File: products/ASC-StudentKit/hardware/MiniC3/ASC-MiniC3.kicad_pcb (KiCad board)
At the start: 2 copper layers, 48 x 44 mm, 36 parts, among them J1 PUMP, J3 AUX, J4 FLOW, J5 I2C, J6 RELAY 230V, K1 HF46F/005-HS1, Q1 AO3400A, Q2 AO3400A, U1 ESP32-C3 Super Mini, U2 DS1307Z+, Y1 32.768k 12.5pF

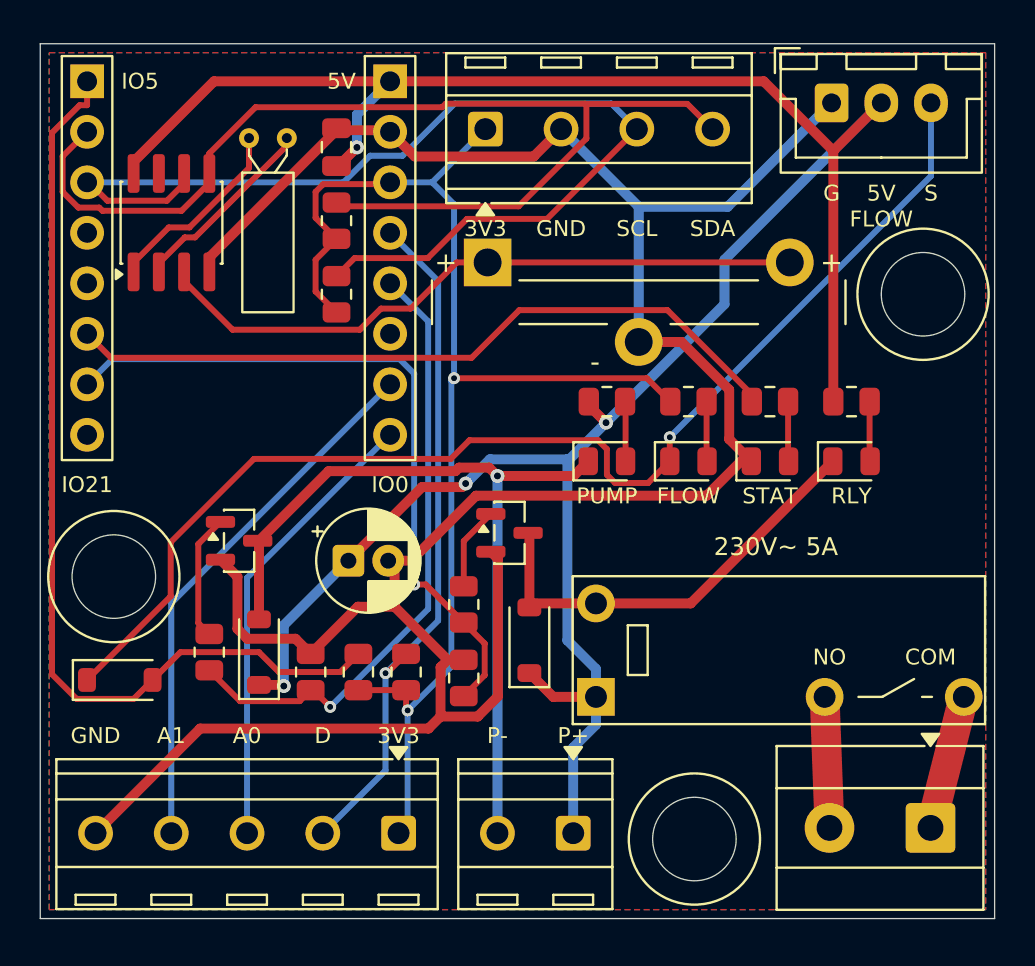
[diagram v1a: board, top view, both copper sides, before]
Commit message: ASC Mini-C3: ULN2003A driver, combo flow connector, assembly markings
- ULN2003A (LCSC C7512) drives the pump (ch 1+2) and the relay (ch 3);
  replaces 2 x AO3400A, 3 x B5819W and 4 resistors, as on FG1
- Flow input: one footprint takes a JST-XH (bench) or a 3.5 mm 3-pole
  screw terminal (FG1 field cable)
- Screw terminals now Phoenix PT-1,5 3.5 mm (KF350 type, library 3D);
  relay output is a pluggable MSTBVA 5.08 header like FG1's
- 1206 LEDs for hand soldering; ref + value labels on every part
  (R3 1K, U3 ULN2003 ...), "1" at IC pin 1, "+" at LED/diode anodes;
  back reads "Agri Sensors and Controls  Oct 2026"
- Re-routed, DRC clean (mains 5 mm), panel and fab regenerated
- Sourcing BOM: 1206 LED and ULN2003A LCSC numbers, CR2032 holder as an
  alternative to the tabbed cell; kit about Rs 967

Co-Authored-By: Claude Opus 5.5 <noreply@anthropic.com>
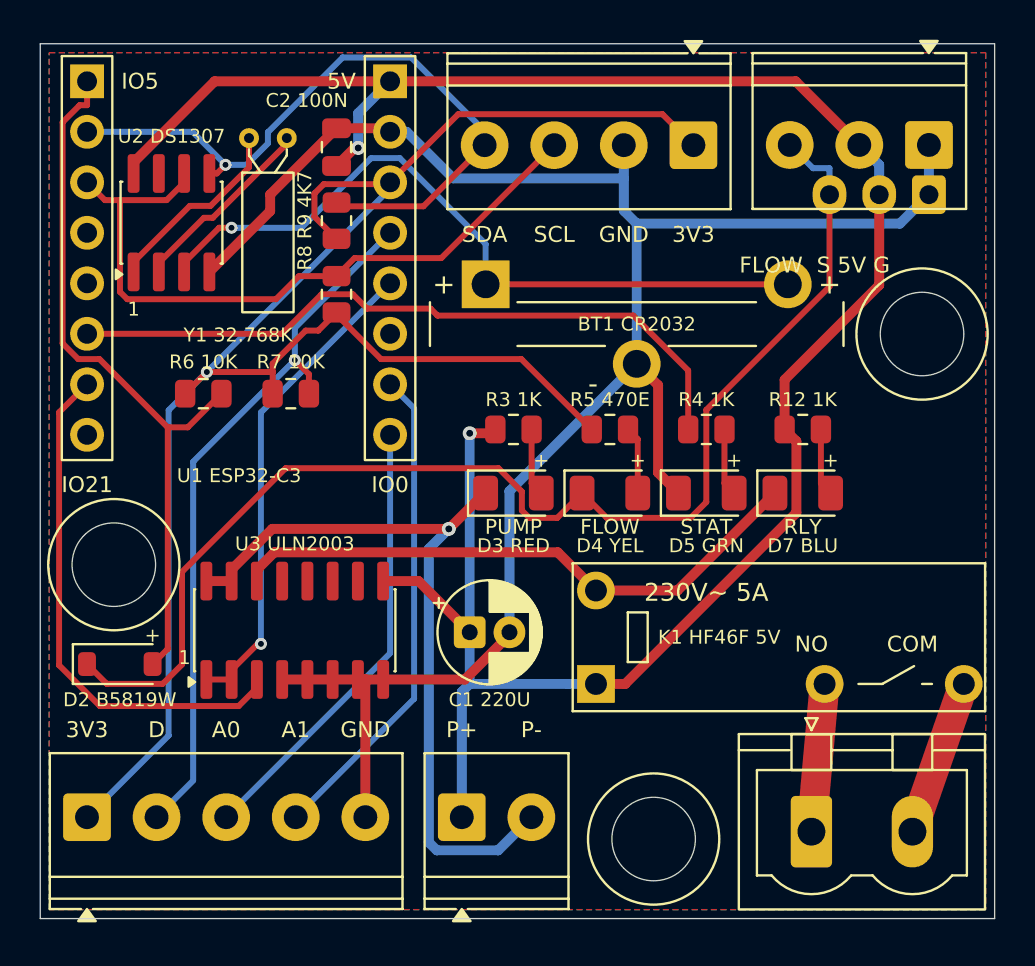
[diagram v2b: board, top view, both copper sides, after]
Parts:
- removed D1, D6: B5819W, Diode_SMD:D_SOD-123
- removed Q1, Q2: AO3400A, Package_TO_SOT_SMD:SOT-23
- removed R1, R10: 100, Resistor_SMD:R_0805_2012Metric
- removed R11, R2: 100k, Resistor_SMD:R_0805_2012Metric
- added U3: ULN2003A, Package_SO:SOIC-16_3.9x9.9mm_P1.27mm, F.Cu at (112.8, 89.5)
- D3, D4, D5, D7: footprint LED_SMD:LED_0805_2012Metric -> LED_SMD:LED_1206_3216Metric
- J1: footprint TerminalBlock_MetzConnect:TerminalBlock_MetzConnect_Type086_RT03402HBLC_1x02_P3.81mm_Horizontal -> TerminalBlock_Phoenix:TerminalBlock_Phoenix_PT-1,5-2-3.5-H_1x02_P3.50mm_Horizontal
- J3: footprint TerminalBlock_MetzConnect:TerminalBlock_MetzConnect_Type086_RT03405HBLC_1x05_P3.81mm_Horizontal -> TerminalBlock_Phoenix:TerminalBlock_Phoenix_PT-1,5-5-3.5-H_1x05_P3.50mm_Horizontal
- J4: value FLOW -> FLOW (XH or 3.5 mm); footprint Connector_JST:JST_XH_B3B-XH-A_1x03_P2.50mm_Vertical -> ASC:Flow_XH3_or_PT-1,5-3-3.5mm
- J5: footprint TerminalBlock_MetzConnect:TerminalBlock_MetzConnect_Type086_RT03404HBLC_1x04_P3.81mm_Horizontal -> TerminalBlock_Phoenix:TerminalBlock_Phoenix_PT-1,5-4-3.5-H_1x04_P3.50mm_Horizontal
- J6: value RELAY 230V -> RELAY 230V (MSTBVA); footprint TerminalBlock_MetzConnect:TerminalBlock_MetzConnect_Type101_RT01602HBWC_1x02_P5.08mm_Horizontal -> Connector_Phoenix_MSTB:PhoenixContact_MSTBVA_2,5_2-G-5,08_1x02_P5.08mm_Vertical
- moved R6 16.0 mm to (108.2, 77.6), turned to 0 degrees
- moved J3 15.7 mm to (102.3, 98.9), turned to 0 degrees
- moved R7 15.2 mm to (112.6, 77.6), turned to 0 degrees
- moved J5 10.5 mm to (132.8, 65.1), turned to 180 degrees
- moved C1 7.08 mm to (121.6, 89.6)
- moved J6 5.99 mm to (138.8, 99.6), turned to 0 degrees
- moved J1 5.66 mm to (121.2, 98.9), turned to 0 degrees
- moved J4 5.33 mm to (144.7, 65.1), turned to 180 degrees
- moved D3 4.96 mm to (123.8, 82.6)
- moved R3 4.90 mm to (123.8, 79.4)
- moved D4 4.26 mm to (128.7, 82.6)
- moved R5 4.19 mm to (128.7, 79.4)
- moved D5 3.58 mm to (133.5, 82.6)
- moved R4 3.49 mm to (133.5, 79.4)
- moved D7 2.93 mm to (138.3, 82.6)
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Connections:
- J6 pad 1: /RELAY_COM -> /RELAY_NO
- J6 pad 2: /RELAY_NO -> /RELAY_COM
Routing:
- net GND: track 129.9 -> 97.4 mm
- net +3V3: track 66.4 -> 88.3 mm, vias 2 -> 1
- net /SDA: track 56.0 -> 35.3 mm, vias 0 -> 1
- net +5V: track 132.1 -> 112.9 mm, vias 4 -> 2
- net /SCL: track 54.1 -> 35.9 mm
- net /FLOW: track 48.5 -> 36.6 mm
- net /RELAY: track 35.7 -> 26.3 mm, vias 1 -> 0
- net /RELAY_COIL: track 22.0 -> 29.8 mm
- net /PUMP: track 31.4 -> 24.6 mm
- net /PUMP_G: track 6.33 -> 0.00 mm
- net /RELAY_G: track 4.20 -> 0.00 mm
- net /VBAT: track 33.3 -> 36.8 mm, vias 0 -> 1
- net /AUX_A1: track 27.1 -> 24.7 mm
- net /PUMP_N: track 40.5 -> 38.4 mm
- net /FLOW_EXT: track 61.5 -> 63.6 mm, vias 1 -> 0
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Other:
- board text added: "+"
- board text added: "1"
- board text added: "Agri Sensors and Controls Oct 2026"
- board text added: "BT1 CR2032"
- board text added: "C1 220U"
- board text added: "C2 100N"
- board text added: "D2 B5819W"
- board text added: "D3 RED"
- board text added: "D4 YEL"
- board text added: "D5 GRN"
- board text added: "D7 BLU"
- board text added: "FLOW S 5V G"
- board text added: "K1 HF46F 5V"
- board text added: "R12 1K"
- board text added: "R3 1K"
- board text added: "R4 1K"
- board text added: "R5 470E"
- board text added: "R6 10K"
- board text added: "R7 10K"
- board text added: "R8 R9 4K7"
- board text added: "U1 ESP32-C3"
- board text added: "U2 DS1307"
- board text added: "U3 ULN2003"
- board text added: "Y1 32.768K"
- board text removed: "5V"
- board text removed: "Agri Sensors and Controls"
- board text removed: "G"
- board text removed: "MAINS BEFORE OPENING"
- board text removed: "RELAY 230 V: DISCONNECT"
- board text removed: "S"

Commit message: ASC Mini-C3: LED colours, relay header turned, date line
- LEDs: PUMP and RLY yellow (C30584802), STATUS red (C37635751),
  FLOW yellow-green (C28310441, ~2 V: it runs from 3.3 V into the
  sensor output); the Super Mini's blue LED on GPIO8 is the WiFi LED
- Relay MSTBVA header turned 180 so the curved side faces inward, as on
  FG1; pins re-mapped (1 COM, 2 NO), mains tracks re-drawn, 5.00 mm
- Back silkscreen: "Oct 2026" on its own line
- Re-routed, DRC clean; panel, fab, BOM/CPL and sourcing regenerated

Co-Authored-By: Claude Opus 5.5 <noreply@anthropic.com>
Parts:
- D3: value PUMP red -> PUMP yellow
- D4: value FLOW yellow -> FLOW yellow-green
- D5: value STATUS green -> STATUS red
- D7: value RELAY blue -> RELAY yellow
- moved J6 5.19 mm to (143.9, 98.6), turned to 180 degrees
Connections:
- J6 pad 1: /RELAY_NO -> /RELAY_COM
- J6 pad 2: /RELAY_COM -> /RELAY_NO
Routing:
- net /SCL: track 35.9 -> 42.0 mm
- net /PUMP_N: track 38.4 -> 43.3 mm
- net /SDA: track 35.3 -> 30.7 mm
- net /VBAT: track 36.8 -> 32.6 mm
- net GND: track 97.4 -> 99.5 mm, vias 0 -> 1
- net +5V: track 112.9 -> 115.0 mm, vias 2 -> 1
- net /RELAY: track 26.3 -> 24.5 mm
- net /XT2: track 9.66 -> 11.2 mm, vias 0 -> 1
- net /AUX_D: track 36.2 -> 37.6 mm
- net /XT1: track 9.74 -> 10.9 mm, vias 0 -> 1
- net /RELAY_NO: track 7.46 -> 6.46 mm
- net /RELAY_COM: track 7.87 -> 6.93 mm
- net /FLOW_EXT: track 63.6 -> 64.5 mm, vias 0 -> 2
- net +3V3: track 88.3 -> 87.5 mm
- net /LED_STATUS: track 35.6 -> 35.0 mm
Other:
- board text added: "Agri Sensors and Controls"
- board text added: "D3 YEL"
- board text added: "D4 GRN"
- board text added: "D5 RED"
- board text added: "D7 YEL"
- board text added: "Oct 2026"
- board text removed: "Agri Sensors and Controls Oct 2026"
- board text removed: "D3 RED"
- board text removed: "D4 YEL"
- board text removed: "D5 GRN"
- board text removed: "D7 BLU"

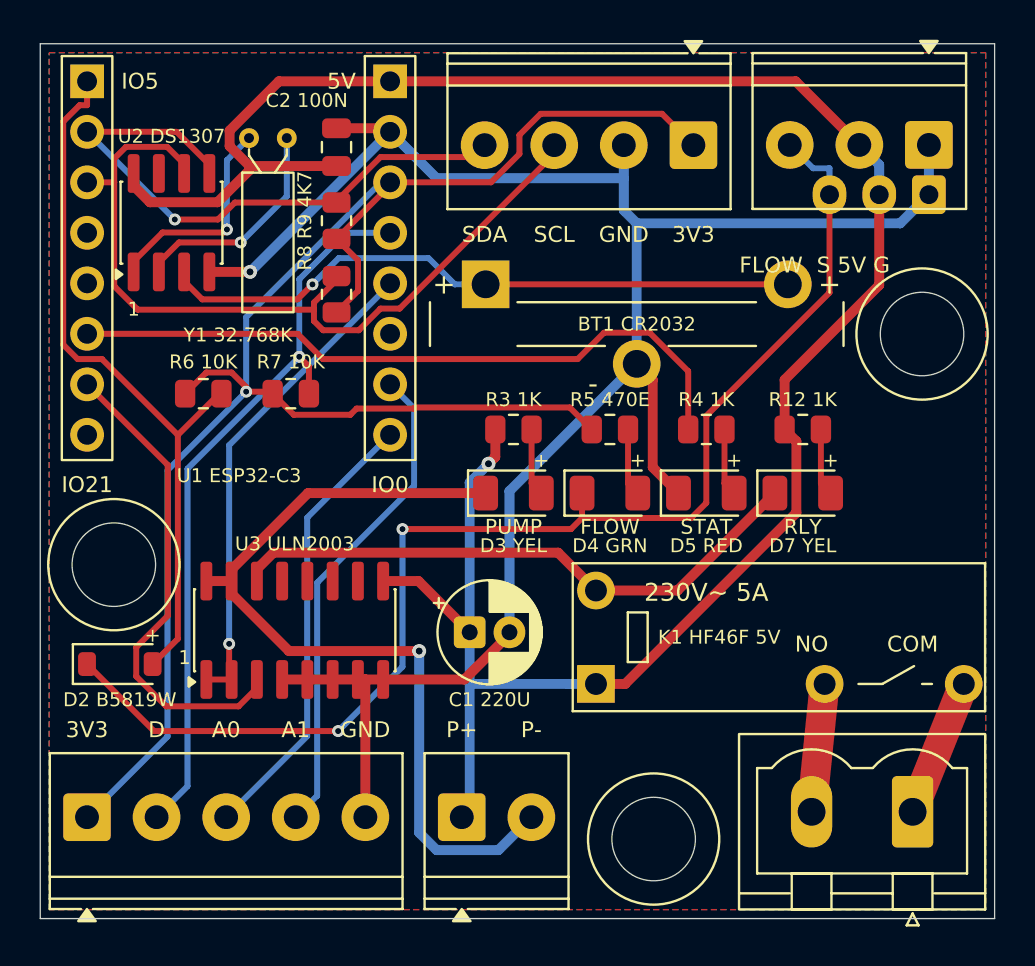
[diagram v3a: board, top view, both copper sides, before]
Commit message: ASC Mini-C3: slot-and-tab panel, flow pinout fix, BOM rates
- Panel now 98 x 98: 4 Minis + 2 AHT20 sticks, 2 mm routed slots with
  tabs and 0.5 mm mouse-bite holes (78, NPTH); no V-cut, as WhyPCB asked
  (JLC charges extra for V-cut). Zip carries a drawing and PANEL-README.
- Flow connector pinout fixed to the YF-S401 wiring: 1 = 5V (red),
  2 = GND (black, middle), 3 = SIG (yellow); silkscreen "FLOW S G 5V".
  Re-routed, DRC clean, mains clearance 5.00 mm.
- BOM: WhyPCB Rs 1,500 / 5 panels, Rs 2,000 / 10 panels (Rs 50 per Mini);
  kit about Rs 979; 2-kit sample about Rs 4,840 + LCSC shipping

Co-Authored-By: Claude Opus 5.5 <noreply@anthropic.com>
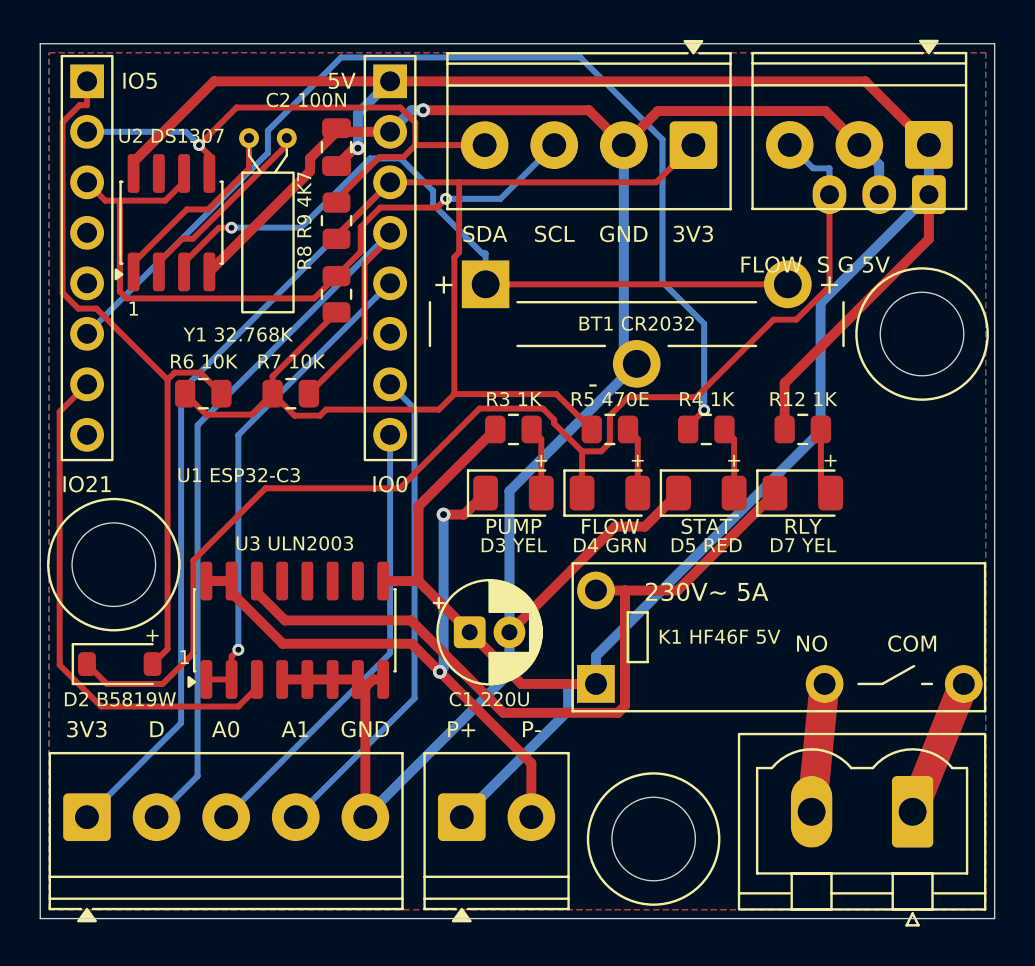
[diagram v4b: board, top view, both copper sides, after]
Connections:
- J4 pad 1: GND -> +5V
- J4 pad 2: +5V -> GND
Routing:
- net /LED_STATUS: track 35.0 -> 52.9 mm, vias 0 -> 1
- net +5V: track 115.0 -> 130.3 mm
- net +3V3: track 87.5 -> 97.4 mm, vias 1 -> 0
- net /PUMP_N: track 43.3 -> 33.7 mm, vias 1 -> 2
- net /RELAY_COIL: track 29.8 -> 38.6 mm
- net /AUX_D: track 37.6 -> 44.0 mm, vias 1 -> 0
- net /SCL: track 42.0 -> 36.6 mm, vias 0 -> 1
- net GND: track 99.5 -> 104.7 mm
- net /VBAT: track 32.6 -> 36.9 mm
- net /FLOW_EXT: track 64.5 -> 62.0 mm, vias 2 -> 0
- net /RELAY: track 24.5 -> 26.3 mm
- net /XT2: track 11.2 -> 9.71 mm, vias 1 -> 0
- net /SDA: track 30.7 -> 29.4 mm
- net /XT1: track 10.9 -> 9.76 mm, vias 1 -> 0
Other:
- board text added: "FLOW S G 5V"
- board text removed: "FLOW S 5V G"
